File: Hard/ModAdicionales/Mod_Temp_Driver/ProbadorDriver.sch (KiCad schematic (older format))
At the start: 8 parts, among them J201 Conn_01x11_Female, J202 Conn_02x05_Odd_Even, J203 Conn_02x10_Odd_Even

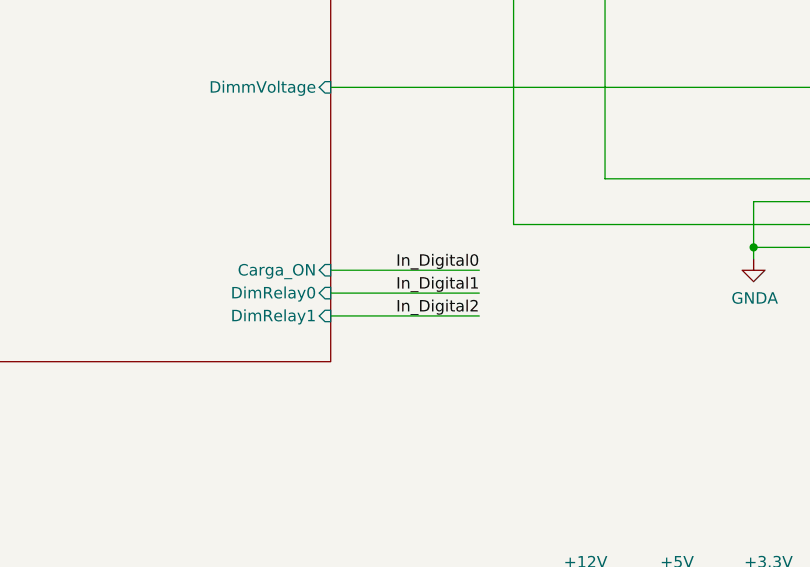
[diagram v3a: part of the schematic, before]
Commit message: Avance en trazado de pistas Modulos Adicionales
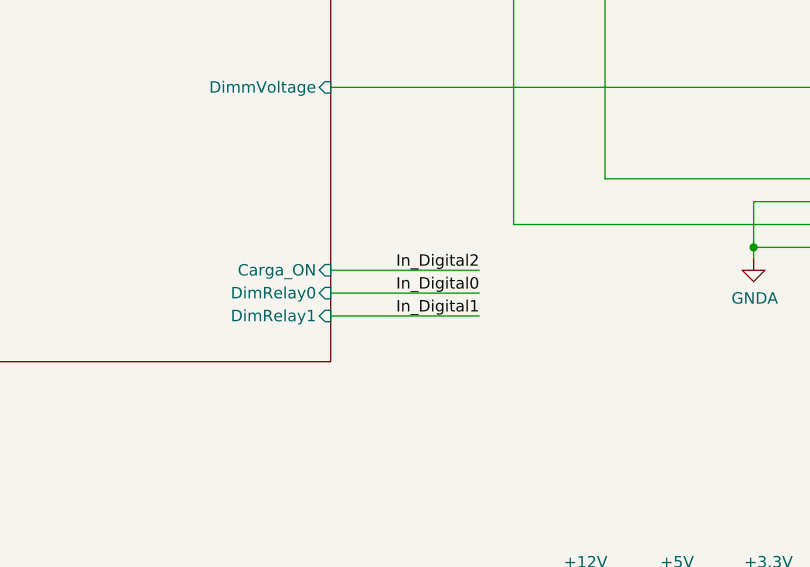
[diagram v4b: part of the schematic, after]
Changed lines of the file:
@@
 Wire Wire Line
 	10550 3850 10550 4350
+Text Label 7200 4750 2    50   ~ 0
+In_Digital0
+Text Label 7200 4850 2    50   ~ 0
+In_Digital1
 Text Label 7200 4650 2    50   ~ 0
-In_Digital0
-Text Label 7200 4750 2    50   ~ 0
-In_Digital1
-Text Label 7200 4850 2    50   ~ 0
 In_Digital2
+Wire Wire Line
+	7200 4750 6550 4750
+Wire Wire Line
+	6550 4850 7200 4850
 Wire Wire Line
 	7200 4650 6550 4650
 Wire Wire Line
-	6550 4750 7200 4750
-Wire Wire Line
-	7200 4850 6550 4850
-Wire Wire Line
 	3950 3700 3300 3700
